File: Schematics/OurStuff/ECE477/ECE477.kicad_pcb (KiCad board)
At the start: 2 copper layers, 105 x 40.5 mm, 65 parts, among them J1 USB_B_Micro, J2 Barrel_Jack, J3 OLED JST PH 7pin, J7 D30V30F3, Q1 SS8050-G, Q2 SS8050-G, U1 ESP32-WROOM-32E, U2 CP2102N-Axx-xQFN28

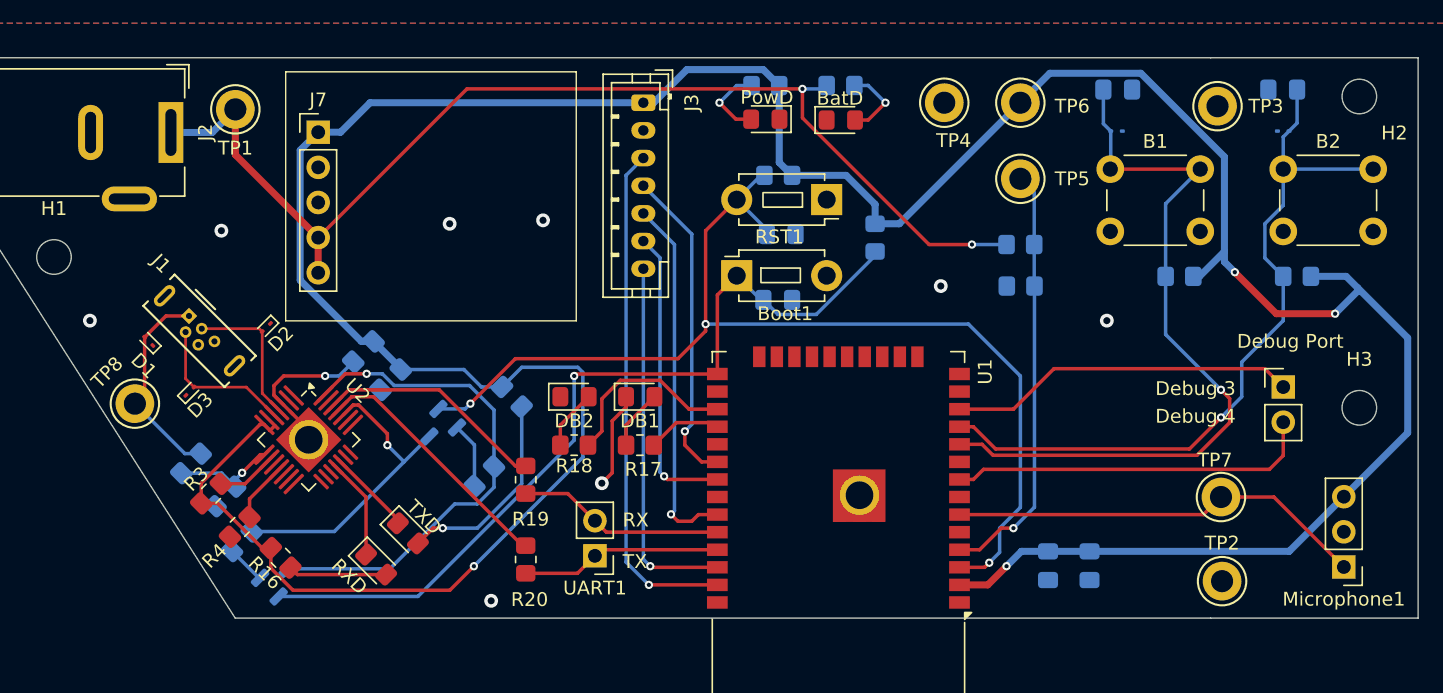
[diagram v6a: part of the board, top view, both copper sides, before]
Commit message: updated PCB with new ESD IC
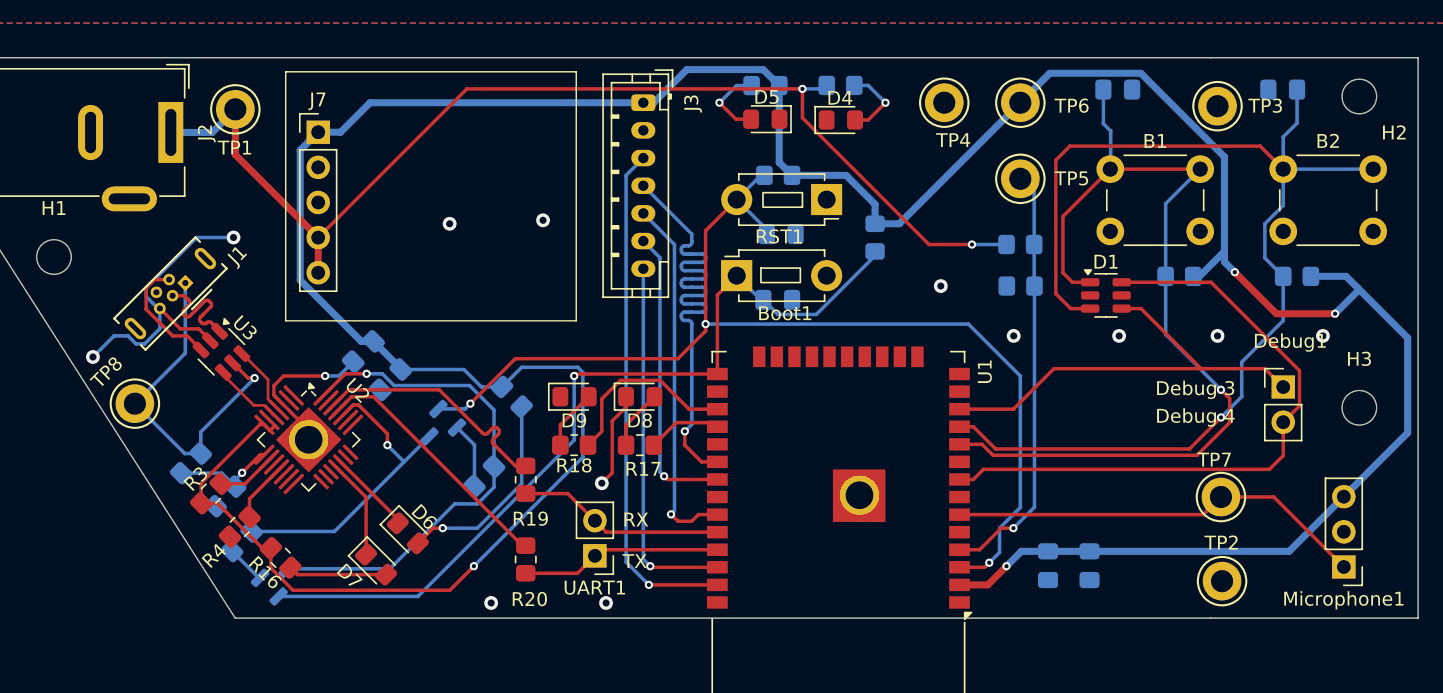
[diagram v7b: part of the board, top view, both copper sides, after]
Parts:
- removed D10, D11, D2, D3: ESD9B5.0ST5G, Diode_SMD:D_SOD-923
- added U3: USBLC6-2SC6, Package_TO_SOT_SMD:SOT-23-6, F.Cu at (118.5, 71.3)
- D1: value ESD9B5.0ST5G -> ESDA6V1BC6; footprint Diode_SMD:D_SOD-923 -> Package_TO_SOT_SMD:SOT-23-6
- Debug1: renamed from Debug Port
- moved D1 69.3 mm to (182.4, 67.2), turned to 0 degrees
- moved J1 2.40 mm to (115.9, 66.3), turned to -135 degrees
- renumbered BatD to D4, PowD to D5, TXD to D6, RXD to D7, DB1 to D8, DB2 to D9
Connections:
- D1 pad 1: Gnd_Bat -> /Button1
- D1 pad 2: V_BUS -> Gnd_Bat
- J1 pad 2: /USB_DN -> Net-(J1-D-)
- J1 pad 3: /USB_DP -> Net-(J1-D+)
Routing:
- net /Button2: track 54.1 -> 84.2 mm
- net Gnd_Bat: track 17.8 -> 39.8 mm, vias 9 -> 13
- net /Debug_4: track 26.5 -> 46.2 mm
- net /O_CLK: track 23.3 -> 36.5 mm
- net /Button1: track 54.6 -> 65.8 mm
- net V_BUS: track 15.2 -> 25.6 mm, vias 0 -> 1
- net Net-(J1-D-): track 0.00 -> 8.64 mm
- net Net-(J1-D+): track 0.00 -> 8.56 mm
- net /Debug_3: track 25.2 -> 32.9 mm
- net /USB_DN: track 11.4 -> 5.20 mm
- net /USB_DP: track 11.2 -> 5.22 mm
- net Net-(U2-TXD): track 17.2 -> 18.8 mm

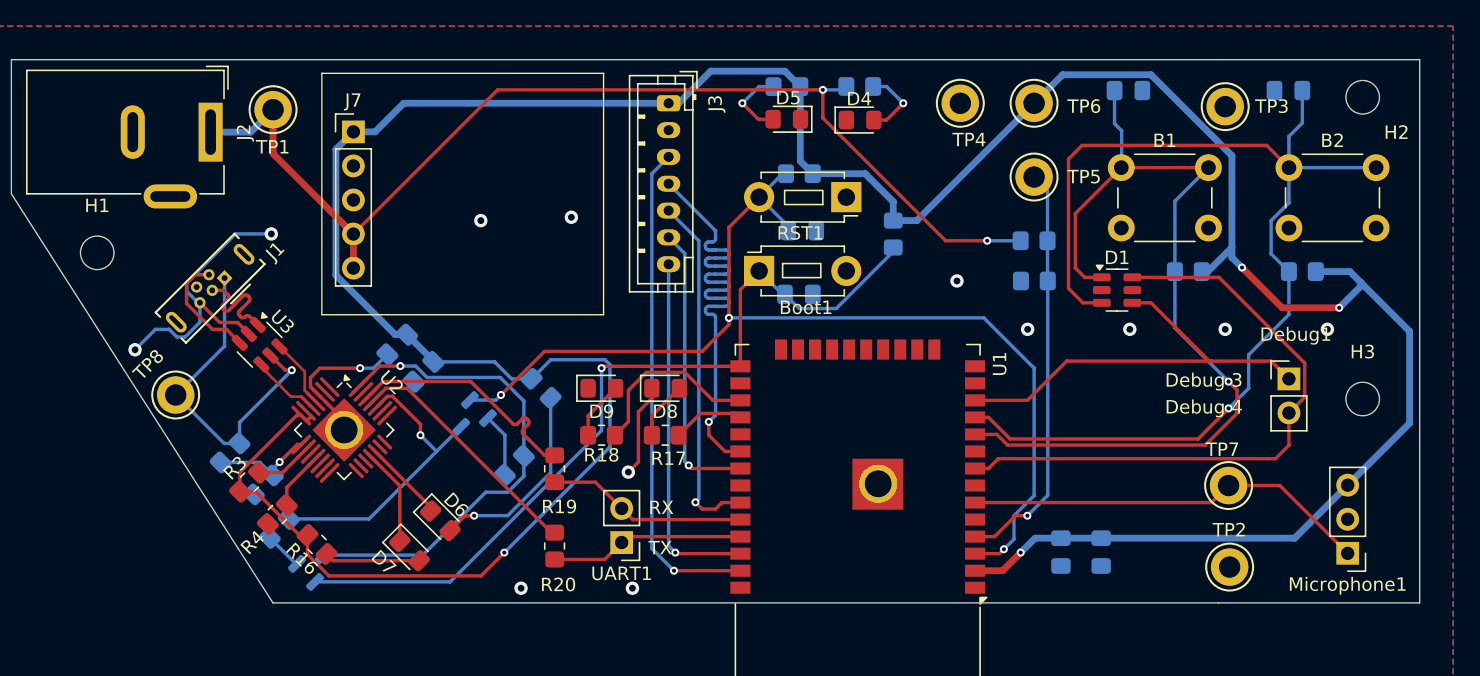
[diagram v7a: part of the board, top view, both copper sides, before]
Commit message: revised changes from dr W feedback
hi
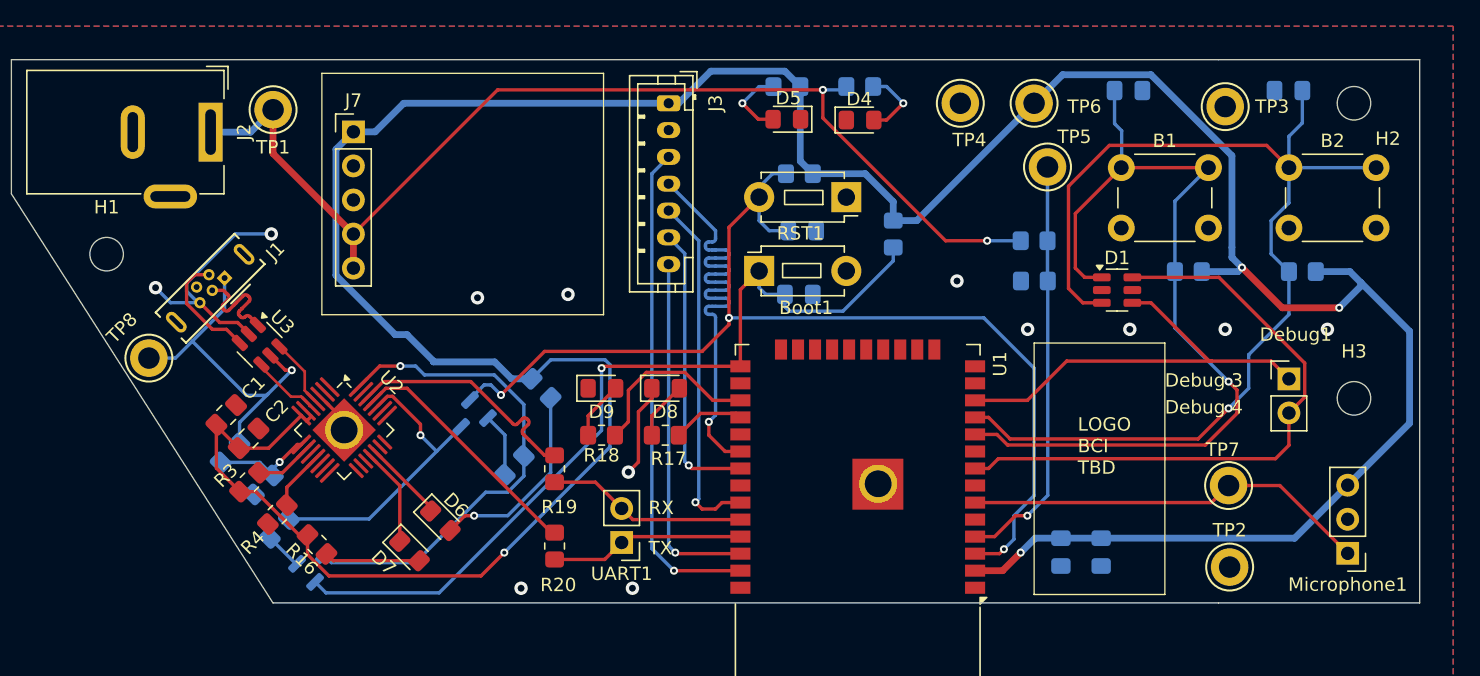
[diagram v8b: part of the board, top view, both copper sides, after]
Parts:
- C1, C2: moved to F.Cu
- moved C2 14.0 mm to (117.7, 78.2), turned to 45 degrees
- moved C1 13.8 mm to (116.0, 76.5), turned to 45 degrees
- moved TP8 3.40 mm to (110.2, 72.2)
- moved TP5 1.25 mm to (177.2, 58.0)
- moved H2 0.79 mm to (200.1, 53.2)
- moved H1 0.71 mm to (107.1, 64.5)
- moved H3 0.65 mm to (200.1, 75.2)
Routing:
- net Gnd_Bat: track 39.8 -> 27.8 mm, vias 13 -> 12
- net +3.3V: track 244.1 -> 250.3 mm
- net /IO0: track 62.0 -> 64.5 mm
- net /EN: track 79.2 -> 81.2 mm
- net /Button2: track 84.2 -> 83.0 mm
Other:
- board text added: "ECE 477 Team 2: Alfredo Barandearan Ben Miller Emery Bredemeyer Rohit Lala"
- board text added: "LOGO BCI TBD"
